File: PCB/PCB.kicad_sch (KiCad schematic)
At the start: 8 parts, among them U1 STM8S003F3P, U2 D168K

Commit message: Rev 0.11 of schematic, rev 0.1 of layout
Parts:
- added U2: PCB-USB-PWR-connector, PCB-USB:PCB-USB-PWR-connector, symbol PCB-USB:PCB-USB-PWR-connector
- C1: footprint (none) -> Capacitor_SMD:C_1206_3216Metric
- C2, C3: footprint (none) -> Capacitor_SMD:C_0603_1608Metric
- C4: footprint (none) -> Capacitor_SMD:C_0805_2012Metric
- R1, R2: footprint (none) -> Resistor_SMD:R_0402_1005Metric
- renumbered U2 to U3
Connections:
- net +5V: now also U2.1 (GND)
- net B: now also U1.20 (PD3); no longer U1.19 (PD2)
- net C: now also U1.19 (PD2); no longer U1.20 (PD3)
- net D: now also U1.14 (PC4); no longer U1.1 (PD4)
- net E: now also U1.12 (PB4); no longer U1.2 (PD5)
- net F: now also U1.13 (PC3); no longer U1.3 (PD6)
- net G: now also U1.11 (PB5); no longer U1.17 (PC7)
- net GND: now also U2.2 (Vcc)
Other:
- moved on the sheet: R1, R2, U3

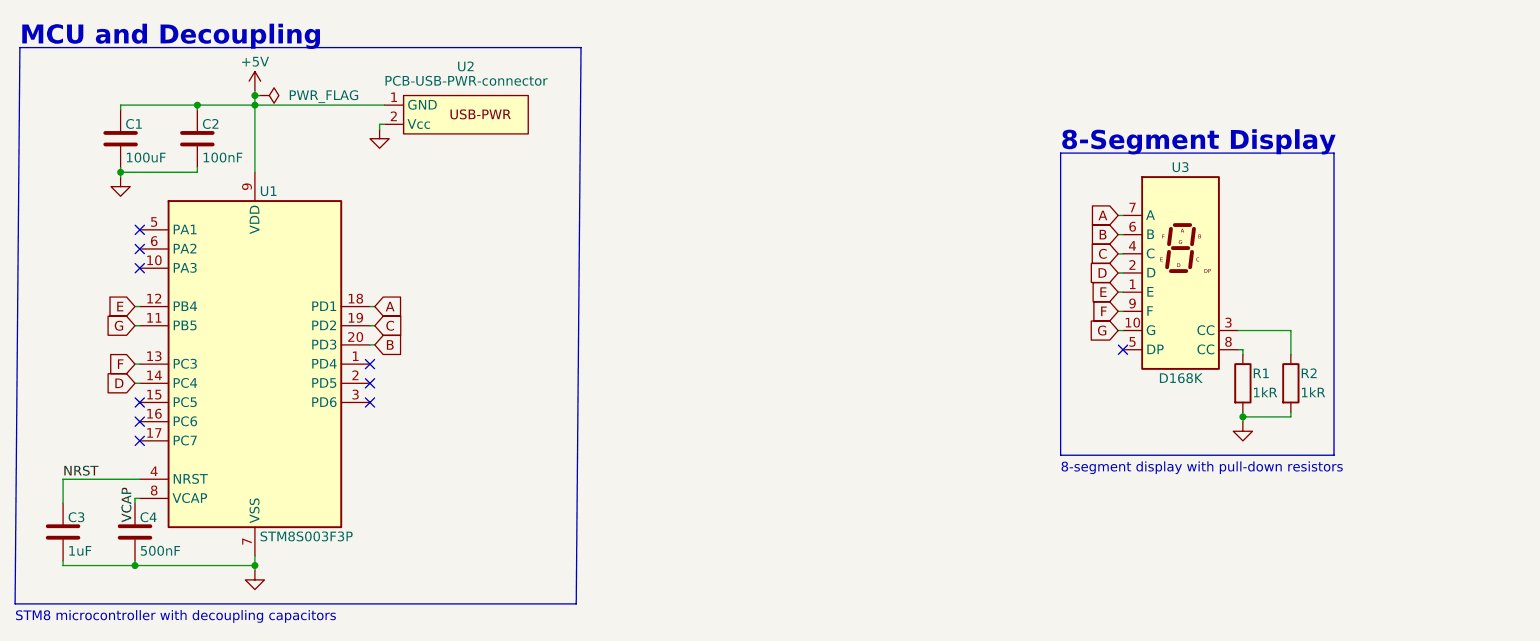
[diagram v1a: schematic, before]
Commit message: PCB revision 0.11: correct decoupling capacitors, change IO routing, Schematic revision 0.12: change IO routing
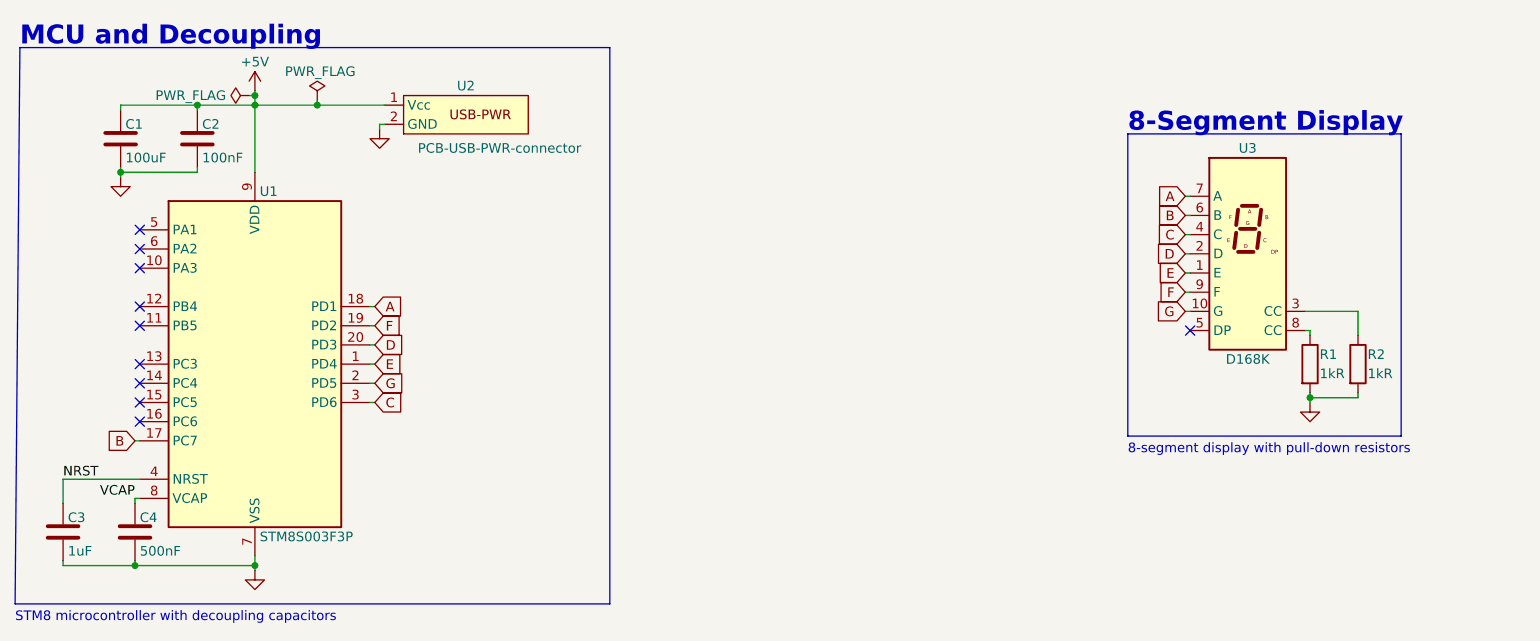
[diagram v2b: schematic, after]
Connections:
- net B: now also U1.17 (PC7); no longer U1.20 (PD3)
- net C: now also U1.3 (PD6); no longer U1.19 (PD2)
- net D: now also U1.20 (PD3); no longer U1.14 (PC4)
- net E: now also U1.1 (PD4); no longer U1.12 (PB4)
- net F: now also U1.19 (PD2); no longer U1.13 (PC3)
- net G: now also U1.2 (PD5); no longer U1.11 (PB5)
- net VCAP: now also C4.1, U1.8 (VCAP)
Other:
- moved on the sheet: R1, R2, U3
